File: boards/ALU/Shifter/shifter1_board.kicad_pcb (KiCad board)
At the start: 4 copper layers, 65 x 100 mm, 100 parts

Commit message: Placement, performed by freerouting
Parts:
- added sh1.decap0_L: , RV523:DECAP, F.Cu at (6.00, 90.0)
- added sh1.decap0_M: , RV523:DECAP, F.Cu at (32.0, 90.0)
- added sh1.decap0_R: , RV523:DECAP, F.Cu at (49.0, 90.0)
- added sh1.decap10_L: , RV523:DECAP, F.Cu at (6.00, 50.0)
- added sh1.decap10_M: , RV523:DECAP, F.Cu at (32.0, 50.0)
- added sh1.decap10_R: , RV523:DECAP, F.Cu at (49.0, 50.0)
- added sh1.decap11_L: , RV523:DECAP, F.Cu at (6.00, 46.0)
- added sh1.decap11_M: , RV523:DECAP, F.Cu at (23.0, 46.0)
- added sh1.decap11_R: , RV523:DECAP, F.Cu at (49.0, 46.0)
- added sh1.decap12_L: , RV523:DECAP, F.Cu at (6.00, 42.0)
- added sh1.decap12_M: , RV523:DECAP, F.Cu at (32.0, 42.0)
- added sh1.decap12_R: , RV523:DECAP, F.Cu at (49.0, 42.0)
- added sh1.decap13_L: , RV523:DECAP, F.Cu at (6.00, 38.0)
- added sh1.decap13_M: , RV523:DECAP, F.Cu at (23.0, 38.0)
- added sh1.decap13_R: , RV523:DECAP, F.Cu at (49.0, 38.0)
- added sh1.decap14_L: , RV523:DECAP, F.Cu at (6.00, 34.0)
- added sh1.decap14_M: , RV523:DECAP, F.Cu at (32.0, 34.0)
- added sh1.decap14_R: , RV523:DECAP, F.Cu at (49.0, 34.0)
- added sh1.decap15_L: , RV523:DECAP, F.Cu at (6.00, 30.0)
- added sh1.decap15_M: , RV523:DECAP, F.Cu at (23.0, 30.0)
- added sh1.decap15_R: , RV523:DECAP, F.Cu at (49.0, 30.0)
- added sh1.decap16_L: , RV523:DECAP, F.Cu at (6.00, 26.0)
- added sh1.decap16_M: , RV523:DECAP, F.Cu at (32.0, 26.0)
- added sh1.decap16_R: , RV523:DECAP, F.Cu at (49.0, 26.0)
- added sh1.decap17_L: , RV523:DECAP, F.Cu at (6.00, 22.0)
- added sh1.decap17_M: , RV523:DECAP, F.Cu at (23.0, 22.0)
- added sh1.decap17_R: , RV523:DECAP, F.Cu at (49.0, 22.0)
- added sh1.decap18_L: , RV523:DECAP, F.Cu at (6.00, 18.0)
- added sh1.decap18_M: , RV523:DECAP, F.Cu at (32.0, 18.0)
- added sh1.decap18_R: , RV523:DECAP, F.Cu at (49.0, 18.0)
- added sh1.decap19_L: , RV523:DECAP, F.Cu at (6.00, 14.0)
- added sh1.decap19_M: , RV523:DECAP, F.Cu at (23.0, 14.0)
- added sh1.decap19_R: , RV523:DECAP, F.Cu at (49.0, 14.0)
- added sh1.decap1_L: , RV523:DECAP, F.Cu at (6.00, 86.0)
- added sh1.decap1_M: , RV523:DECAP, F.Cu at (23.0, 86.0)
- added sh1.decap1_R: , RV523:DECAP, F.Cu at (49.0, 86.0)
- added sh1.decap20_L: , RV523:DECAP, F.Cu at (6.00, 10.0)
- added sh1.decap20_M: , RV523:DECAP, F.Cu at (32.0, 10.0)
- added sh1.decap20_R: , RV523:DECAP, F.Cu at (49.0, 10.0)
- added sh1.decap21_L: , RV523:DECAP, F.Cu at (6.00, 6.00)
- added sh1.decap21_M: , RV523:DECAP, F.Cu at (23.0, 6.00)
- added sh1.decap21_R: , RV523:DECAP, F.Cu at (49.0, 6.00)
- added sh1.decap2_L: , RV523:DECAP, F.Cu at (6.00, 82.0)
- added sh1.decap2_M: , RV523:DECAP, F.Cu at (32.0, 82.0)
- added sh1.decap2_R: , RV523:DECAP, F.Cu at (49.0, 82.0)
- added sh1.decap3_L: , RV523:DECAP, F.Cu at (6.00, 78.0)
- added sh1.decap3_M: , RV523:DECAP, F.Cu at (23.0, 78.0)
- added sh1.decap3_R: , RV523:DECAP, F.Cu at (49.0, 78.0)
- added sh1.decap4_L: , RV523:DECAP, F.Cu at (6.00, 74.0)
- added sh1.decap4_M: , RV523:DECAP, F.Cu at (32.0, 74.0)
- added sh1.decap4_R: , RV523:DECAP, F.Cu at (49.0, 74.0)
- added sh1.decap5_L: , RV523:DECAP, F.Cu at (6.00, 70.0)
- added sh1.decap5_M: , RV523:DECAP, F.Cu at (23.0, 70.0)
- added sh1.decap5_R: , RV523:DECAP, F.Cu at (49.0, 70.0)
- added sh1.decap6_L: , RV523:DECAP, F.Cu at (6.00, 66.0)
- added sh1.decap6_M: , RV523:DECAP, F.Cu at (32.0, 66.0)
- added sh1.decap6_R: , RV523:DECAP, F.Cu at (49.0, 66.0)
- added sh1.decap7_L: , RV523:DECAP, F.Cu at (6.00, 62.0)
- added sh1.decap7_M: , RV523:DECAP, F.Cu at (23.0, 62.0)
- added sh1.decap7_R: , RV523:DECAP, F.Cu at (49.0, 62.0)
- added sh1.decap8_L: , RV523:DECAP, F.Cu at (6.00, 58.0)
- added sh1.decap8_M: , RV523:DECAP, F.Cu at (32.0, 58.0)
- added sh1.decap8_R: , RV523:DECAP, F.Cu at (49.0, 58.0)
- added sh1.decap9_L: , RV523:DECAP, F.Cu at (6.00, 54.0)
- added sh1.decap9_M: , RV523:DECAP, F.Cu at (23.0, 54.0)
- added sh1.decap9_R: , RV523:DECAP, F.Cu at (49.0, 54.0)
- moved sh1._217_ 76.1 mm to (12.0, 82.0)
- moved sh1._244_ 62.1 mm to (41.0, 58.0)
- moved sh1._192_ 55.6 mm to (41.0, 54.0)
- moved sh1._243_ 48.3 mm to (33.0, 58.0)
- moved sh1._276_ 45.6 mm to (41.0, 62.0)
- moved sh1._212_ 43.2 mm to (8.00, 58.0)
- moved sh1._204_ 42.2 mm to (7.00, 54.0)
- moved sh1._241_ 38.3 mm to (32.0, 62.0)
- moved sh1._275_ 37.0 mm to (41.0, 70.0)
- moved sh1._193_ 35.8 mm to (41.0, 42.0)
- moved sh1._272_ 35.2 mm to (41.0, 74.0)
- moved sh1._211_ 34.7 mm to (41.0, 34.0)
- moved sh1._203_ 34.0 mm to (8.00, 42.0)
- moved sh1._202_ 33.2 mm to (7.00, 26.0)
- moved sh1._191_ 32.0 mm to (33.0, 42.0)
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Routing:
- net B.0: track 0.00 -> 265.4 mm
- net sh1._068_: track 0.00 -> 262.7 mm
- net sh1._069_: track 0.00 -> 238.6 mm
- net B.1: track 0.00 -> 218.6 mm
- net pins.72: track 0.00 -> 210.1 mm, vias 0 -> 1
- net pins.71: track 0.00 -> 208.3 mm, vias 0 -> 1
- net A.21: track 0.00 -> 87.1 mm, vias 0 -> 2
- net A.22: track 0.00 -> 73.6 mm, vias 0 -> 2
- net A.10: track 0.00 -> 71.7 mm, vias 0 -> 1
- net A.15: track 0.00 -> 71.0 mm, vias 0 -> 2
- net A.12: track 0.00 -> 69.3 mm, vias 0 -> 2
- net sh1._049_: track 0.00 -> 66.4 mm
- net A.4: track 0.00 -> 61.6 mm, vias 0 -> 1
- net A.27: track 0.00 -> 61.1 mm, vias 0 -> 3
- net A.16: track 0.00 -> 59.4 mm, vias 0 -> 2
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
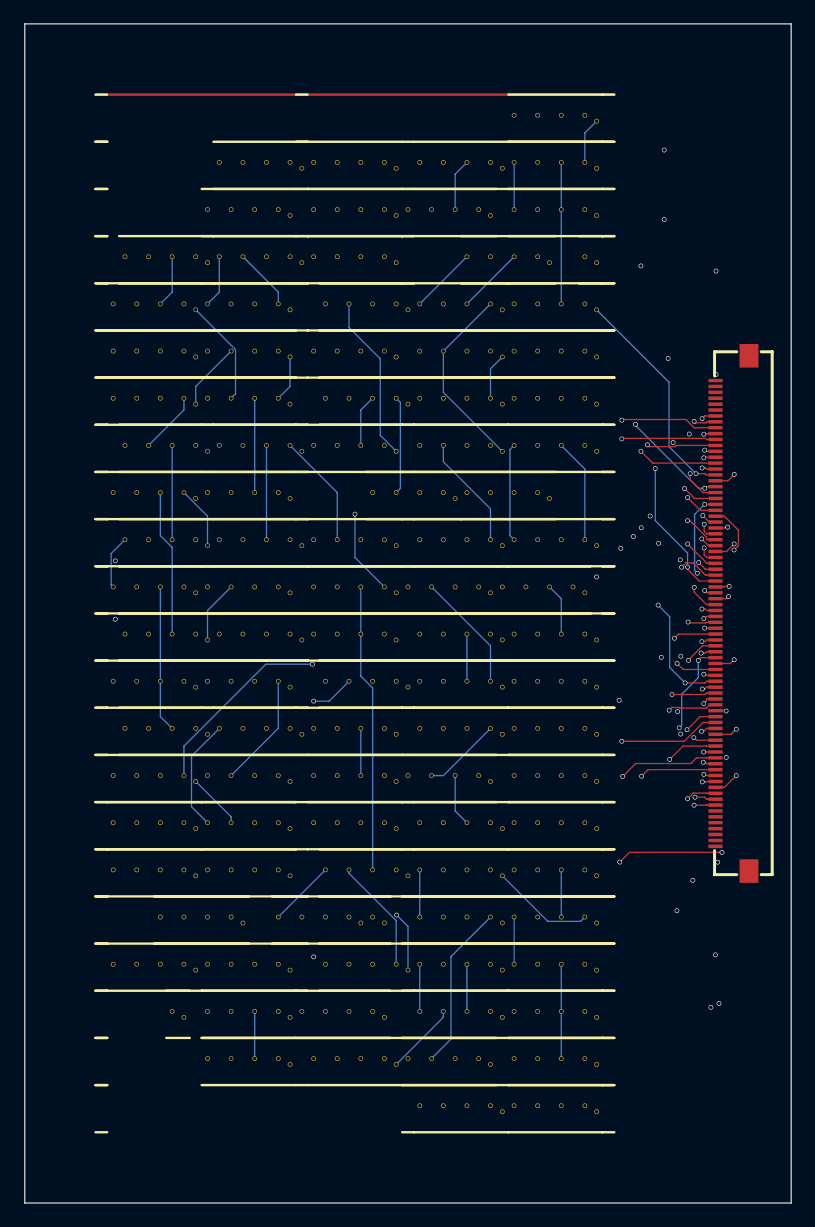
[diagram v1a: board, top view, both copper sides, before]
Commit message: First version of shifter1_board completely routed
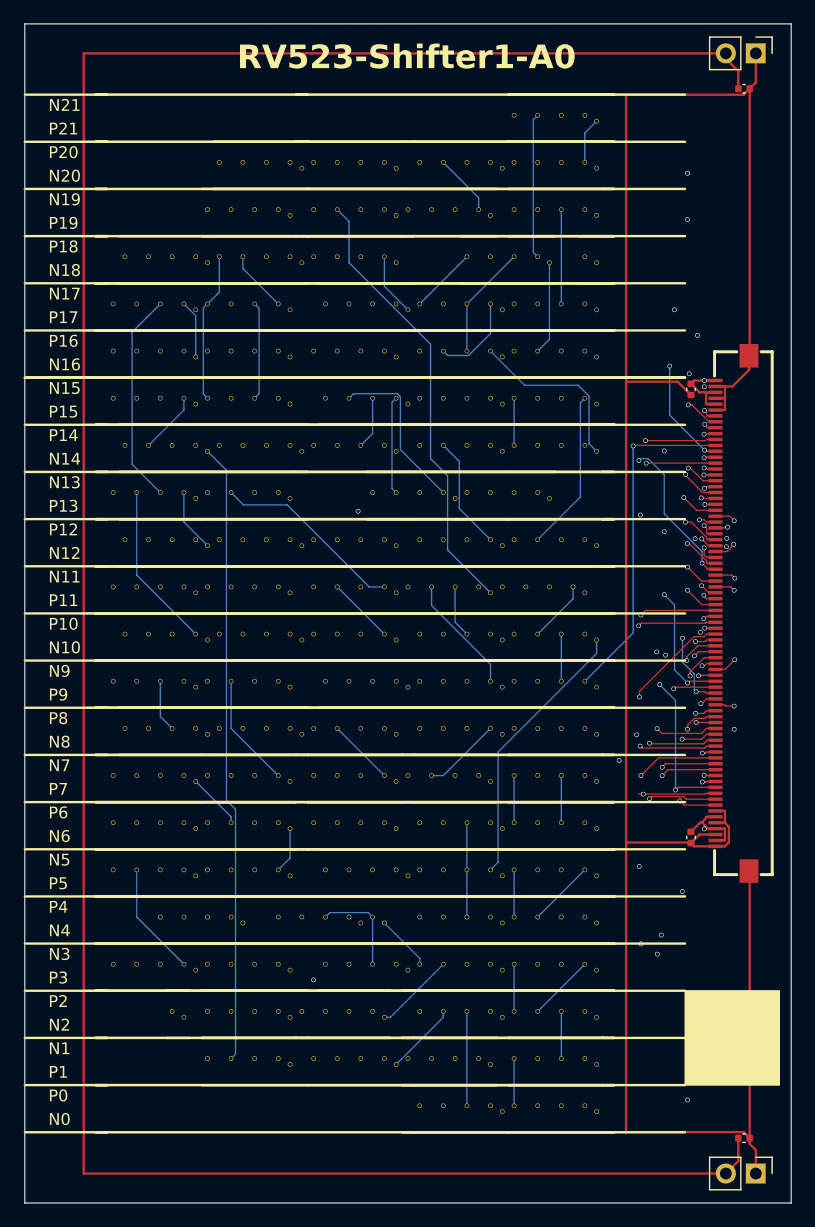
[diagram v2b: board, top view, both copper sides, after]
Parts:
- added C1: , Capacitor_SMD:C_0402_1005Metric, F.Cu at (61.0, 5.50)
- added C2: , Capacitor_SMD:C_0402_1005Metric, F.Cu at (56.5, 31.0)
- added C3: , Capacitor_SMD:C_0402_1005Metric, F.Cu at (56.5, 69.0)
- added C4: , Capacitor_SMD:C_0402_1005Metric, F.Cu at (61.0, 94.5)
- added j2: , Connector_PinHeader_2.54mm:PinHeader_1x02_P2.54mm_Vertical, F.Cu at (62.0, 2.50)
- added j3: , Connector_PinHeader_2.54mm:PinHeader_1x02_P2.54mm_Vertical, F.Cu at (62.0, 97.5)
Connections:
- j1 pad 1: pins.0 -> GND
- j1 pad 2: pins.1 -> VDD
- j1 pad 3: pins.2 -> GND
- j1 pad 4: pins.3 -> VDD
- j1 pad 5: pins.4 -> GND
- j1 pad 6: pins.5 -> VDD
- j1 pad 7: pins.6 -> GND
- j1 pad 75: pins.74 -> GND
- j1 pad 76: pins.75 -> VDD
- j1 pad 77: pins.76 -> GND
- j1 pad 78: pins.77 -> VDD
- j1 pad 79: pins.78 -> GND
- j1 pad 80: pins.79 -> VDD
- j1 pad 81: (no net) -> GND
- j1 pad 82: (no net) -> GND
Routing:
- net VDD: track 0.00 -> 777.6 mm, vias 0 -> 2
- net GND: track 0.00 -> 731.9 mm
- net (no net): track 44.0 -> 0.00 mm
- net sh1._052_: track 38.9 -> 28.9 mm
- net sh1._068_: track 262.7 -> 252.8 mm
- net B.1: track 218.6 -> 226.9 mm
- net A.31: track 48.4 -> 56.1 mm, vias 2 -> 1
- net pins.72: track 210.1 -> 217.7 mm
- net pins.71: track 208.3 -> 215.6 mm
- net F.25: track 36.7 -> 29.8 mm, vias 2 -> 1
- net A.17: track 45.3 -> 39.1 mm, vias 2 -> 1
- net A.27: track 61.1 -> 55.0 mm, vias 3 -> 1
- net A.21: track 87.1 -> 81.4 mm
- net A.23: track 56.4 -> 61.9 mm
- net F.12: track 44.5 -> 39.6 mm
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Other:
- board text added: "N0"
- board text added: "N1"
- board text added: "N10"
- board text added: "N11"
- board text added: "N12"
- board text added: "N13"
- board text added: "N14"
- board text added: "N15"
- board text added: "N16"
- board text added: "N17"
- board text added: "N18"
- board text added: "N19"
- board text added: "N2"
- board text added: "N20"
- board text added: "N21"
- board text added: "N3"
- board text added: "N4"
- board text added: "N5"
- board text added: "N6"
- board text added: "N7"
- board text added: "N8"
- board text added: "N9"
- board text added: "P0"
- board text added: "P1"
- board text added: "P10"
- board text added: "P11"
- board text added: "P12"
- board text added: "P13"
- board text added: "P14"
- board text added: "P15"
- board text added: "P16"
- board text added: "P17"
- board text added: "P18"
- board text added: "P19"
- board text added: "P2"
- board text added: "P20"
- board text added: "P21"
- board text added: "P3"
- board text added: "P4"
- board text added: "P5"
- board text added: "P6"
- board text added: "P7"
- board text added: "P8"
- board text added: "P9"
- board text added: "RV523-Shifter1-A0"

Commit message: Fully routed board, including final board. GND and VDD fill zones
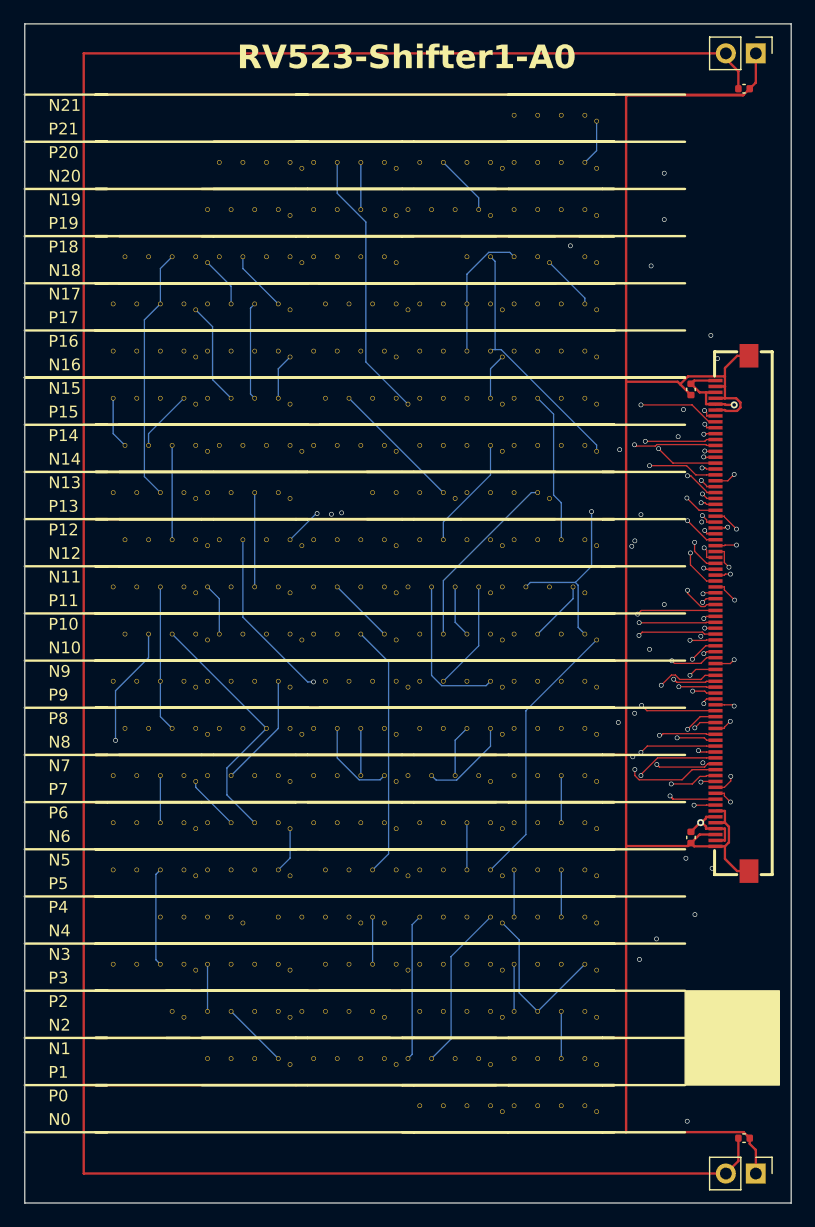
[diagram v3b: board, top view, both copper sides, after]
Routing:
- net GND: track 731.9 -> 707.2 mm
- net sh1._068_: track 252.8 -> 269.3 mm
- net sh1._073_.18: track 32.4 -> 43.9 mm, vias 1 -> 0
- net A.23: track 61.9 -> 71.1 mm, vias 2 -> 3
- net sh1._039_: track 19.7 -> 28.9 mm, vias 0 -> 1
- net sh1._073_.2: track 22.3 -> 30.9 mm
- net pins.71: track 215.6 -> 207.0 mm
- net sh1._063_: track 53.8 -> 61.8 mm, vias 0 -> 1
- net A.21: track 81.4 -> 88.4 mm
- net F.19: track 46.0 -> 53.0 mm
- net A.16: track 62.7 -> 68.9 mm
- net F.23: track 43.7 -> 37.8 mm, vias 2 -> 1
- net A.15: track 68.3 -> 62.6 mm
- net F.11: track 44.6 -> 50.1 mm
- net B.0: track 264.6 -> 259.7 mm
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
